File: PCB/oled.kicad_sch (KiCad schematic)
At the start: 5 parts

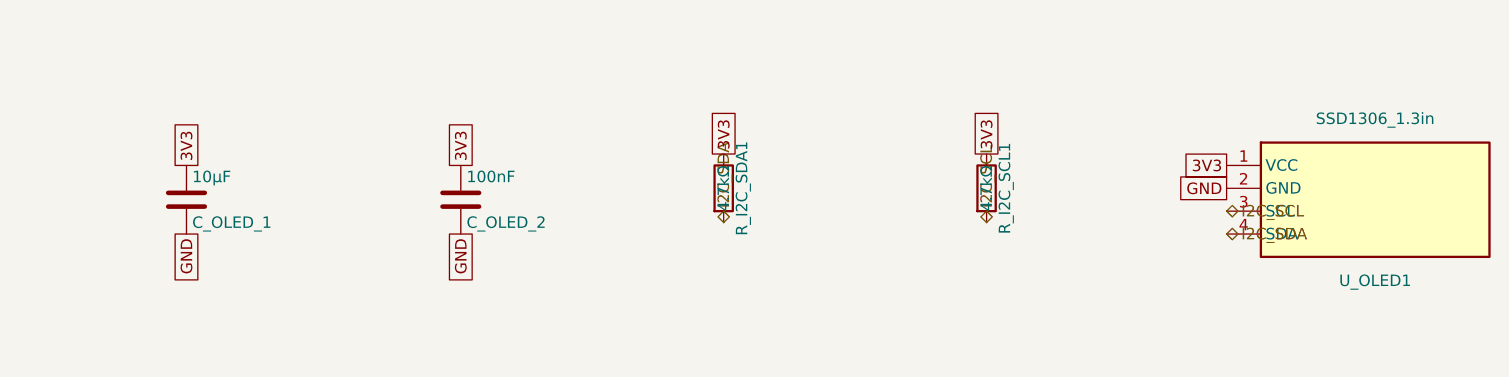
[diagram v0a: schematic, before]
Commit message: Fix footprints and begin layout (#17)
* refactor: updated gulikit footprint

This updates the gulikit thumbstick footprint to be accurate.

* layout: beginning pcb layout

This updates the schematic with a few different footprints while also starts the layout.
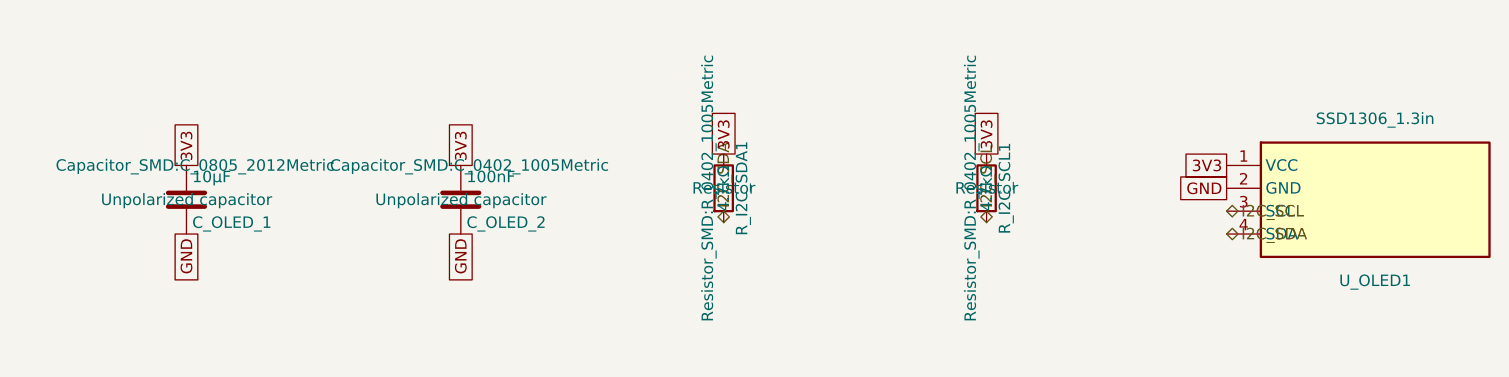
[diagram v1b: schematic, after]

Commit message: refactor: swap footprints and add symmetry
This updates the footprints of a couple components to be smaller and closer to what we want. It also adds two buttons to ensure left and right side symmetry.
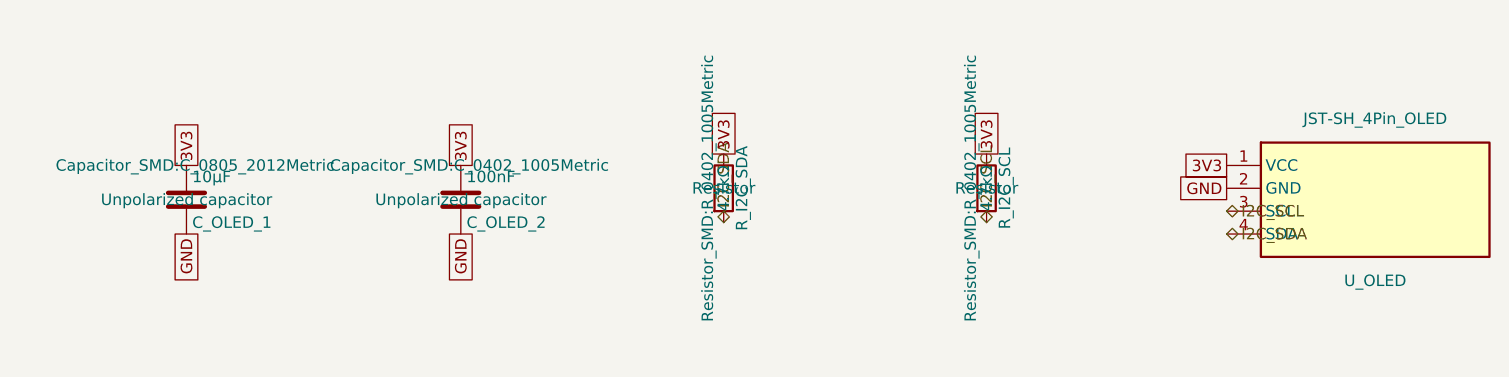
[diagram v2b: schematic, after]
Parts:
- removed R_I2C_SCL1, R_I2C_SDA1: 4.7kΩ, Resistor_SMD:R_0402_1005Metric, symbol Device:R
- removed U_OLED1: SSD1306_1.3in, Display:Adafruit_SSD1306, symbol SnipsControllers:SSD1306_OLED_4pin
- added R_I2C_SCL, R_I2C_SDA: 4.7kΩ, Resistor_SMD:R_0402_1005Metric, symbol Device:R
- added U_OLED: JST-SH_4Pin_OLED, Connector_JST:JST_SH_SM04B-SRSS-TB_1x04-1MP_P1.00mm_Horizontal, symbol SnipsControllers:SSD1306_OLED_4pin
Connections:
- net 3V3: now also R_I2C_SCL.1, R_I2C_SDA.1, U_OLED.1 (VCC)
- net GND: now also U_OLED.2 (GND)
- net I2C_SCL: now also R_I2C_SCL.2, U_OLED.3 (SCL)
- net I2C_SDA: now also R_I2C_SDA.2, U_OLED.4 (SDA)

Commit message: layout: everything is on the board
The board edge cuts are down to 100mm x 35mm. All the components have the right footprints and are on the board, but no traces exist yet, and not all circuits are laid out properly yet. Lots of DRC warnings.
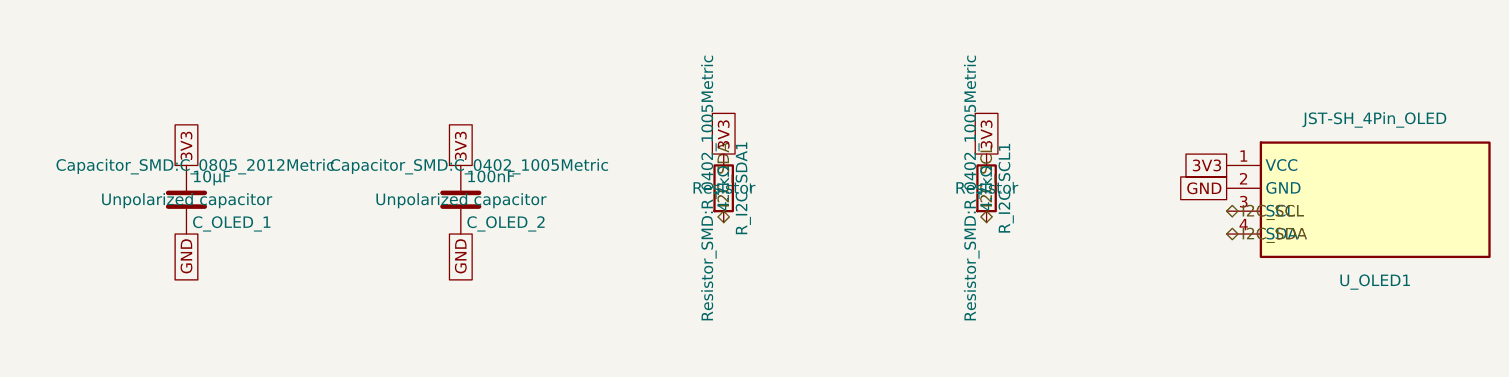
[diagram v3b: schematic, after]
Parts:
- removed R_I2C_SCL, R_I2C_SDA: 4.7kΩ, Resistor_SMD:R_0402_1005Metric, symbol Device:R
- removed U_OLED: JST-SH_4Pin_OLED, Connector_JST:JST_SH_SM04B-SRSS-TB_1x04-1MP_P1.00mm_Horizontal, symbol SnipsControllers:SSD1306_OLED_4pin
- added R_I2C_SCL1, R_I2C_SDA1: 4.7kΩ, Resistor_SMD:R_0402_1005Metric, symbol Device:R
- added U_OLED1: JST-SH_4Pin_OLED, Connector_JST:JST_SH_SM04B-SRSS-TB_1x04-1MP_P1.00mm_Horizontal, symbol SnipsControllers:SSD1306_OLED_4pin
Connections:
- net 3V3: now also R_I2C_SCL1.1, R_I2C_SDA1.1, U_OLED1.1 (VCC)
- net GND: now also U_OLED1.2 (GND)
- net I2C_SCL: now also R_I2C_SCL1.2, U_OLED1.3 (SCL)
- net I2C_SDA: now also R_I2C_SDA1.2, U_OLED1.4 (SDA)

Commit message: task: board is fully routed
That was a pain, but it is all routed and connected now.
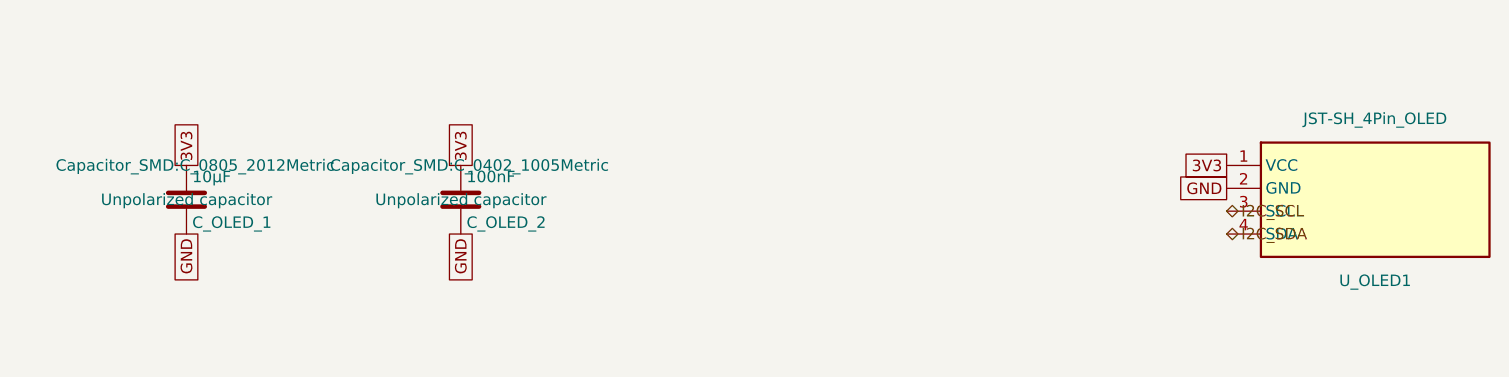
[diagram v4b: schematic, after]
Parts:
- removed R_I2C_SCL1, R_I2C_SDA1: 4.7kΩ, Resistor_SMD:R_0402_1005Metric, symbol Device:R
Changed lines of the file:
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@@
-		)
-	)
-	(global_label "3V3"
-		(shape passive)
-		(at 171.45 100.33 90)
-		(fields_autoplaced yes)
-		(effects
-			(font
-				(size 1.27 1.27)
-			)
-			(justify left)
-		)
-		(property "Intersheetrefs" "${INTERSHEET_REFS}"
-			(at 171.45 100.33 0)
-			(hide yes)
-			(show_name no)
-			(do_not_autoplace no)
-			(effects
-				(font
-					(size 1.27 1.27)
-				)
-			)
-		)
-	)
-	(global_label "3V3"
-		(shape passive)
-		(at 142.24 100.33 90)
-		(fields_autoplaced yes)
-		(effects
-			(font
-				(size 1.27 1.27)
-			)
-			(justify left)
-		)
-		(property "Intersheetrefs" "${INTERSHEET_REFS}"
-			(at 142.24 100.33 0)
-			(hide yes)
-			(show_name no)
-			(do_not_autoplace no)
-			(effects
-				(font
-					(size 1.27 1.27)
-				)
-			)
 		)
 	)
@@
 		(shape bidirectional)
 		(at 198.12 109.22 0)
-		(effects
-			(font
-				(size 1.27 1.27)
-			)
-			(justify left)
-		)
-	)
-	(hierarchical_label "I2C_SDA"
-		(shape bidirectional)
-		(at 142.24 107.95 90)
-		(effects
-			(font
-				(size 1.27 1.27)
-			)
-			(justify left)
-		)
-	)
-	(hierarchical_label "I2C_SCL"
-		(shape bidirectional)
-		(at 171.45 107.95 90)
 		(effects
 			(font
@@
 					(unit 1)
 				)
-			)
-		)
-	)
-	(symbol
-		(lib_id "Device:R")
-		(at 171.45 104.14 0)
-		(unit 1)
-		(body_style 1)
-		(exclude_from_sim no)
-		(in_bom yes)
-		(on_board yes)
-		(in_pos_files yes)
-		(dnp no)
-		(fields_autoplaced yes)
-		(property "Reference" "R_I2C_SCL1"
-			(at 173.482 104.14 90)
-			(show_name no)
-			(do_not_autoplace no)
-			(effects
-				(font
-					(size 1.27 1.27)
-				)
-			)
-		)
-		(property "Value" "4.7kΩ"
-			(at 171.45 104.14 90)
-			(show_name no)
-			(do_not_autoplace no)
-			(effects
-				(font
-					(size 1.27 1.27)
-				)
-			)
-		)
-		(property "Footprint" "Resistor_SMD:R_0402_1005Metric"
-			(at 169.672 104.14 90)
-			(show_name no)
-			(do_not_autoplace no)
-			(effects
-				(font
-					(size 1.27 1.27)
-				)
-			)
-		)
-		(property "Datasheet" ""
-			(at 171.45 104.14 0)
-			(show_name no)
-			(do_not_autoplace no)
-			(effects
-				(font
-					(size 1.27 1.27)
-				)
-			)
-		)
-		(property "Description" "Resistor"
-			(at 171.45 104.14 0)
-			(show_name no)
-			(do_not_autoplace no)
-			(effects
-				(font
-					(size 1.27 1.27)
-				)
-			)
-		)
-		(pin "1"
-		)
-		(pin "2"
-		)
-		(instances
-			(project "snips_controller"
-				(path "/21935953-32a0-46ad-8079-8177920c6978/ab30dd66-bbd7-4b32-bf8e-8b7d2bf83841"
-					(reference "R_I2C_SCL1")
-					(unit 1)
-				)
-			)
-		)
-	)
-	(symbol
-		(lib_id "Device:R")
-		(at 142.24 104.14 0)
-		(unit 1)
-		(body_style 1)
-		(exclude_from_sim no)
-		(in_bom yes)
-		(on_board yes)
-		(in_pos_files yes)
-		(dnp no)
-		(fields_autoplaced yes)
-		(property "Reference" "R_I2C_SDA1"
-			(at 144.272 104.14 90)
-			(show_name no)
-			(do_not_autoplace no)
-			(effects
-				(font
-					(size 1.27 1.27)
-				)
-			)
-		)
-		(property "Value" "4.7kΩ"
-			(at 142.24 104.14 90)
-			(show_name no)
-			(do_not_autoplace no)
-			(effects
-				(font
-					(size 1.27 1.27)
-				)
-			)
-		)
-		(property "Footprint" "Resistor_SMD:R_0402_1005Metric"
-			(at 140.462 104.14 90)
-			(show_name no)
-			(do_not_autoplace no)
-			(effects
-				(font
-					(size 1.27 1.27)
-				)
-			)
-		)
-		(property "Datasheet" ""
-			(at 142.24 104.14 0)
-			(show_name no)
-			(do_not_autoplace no)
-			(effects
-				(font
-					(size 1.27 1.27)
-				)
-			)
-		)
-		(property "Description" "Resistor"
-			(at 142.24 104.14 0)
-			(show_name no)
-			(do_not_autoplace no)
-			(effects
-				(font
-					(size 1.27 1.27)
-				)
-			)
-		)
-		(pin "1"
-		)
-		(pin "2"
-		)
-		(instances
-			(project "snips_controller"
-				(path "/21935953-32a0-46ad-8079-8177920c6978/ab30dd66-bbd7-4b32-bf8e-8b7d2bf83841"
-					(reference "R_I2C_SDA1")
-					(unit 1)
-				)

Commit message: task: part number populated (#26)
kicad-happy run part 2 - MPN numbers populated
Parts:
- C_OLED_1: MF (none) -> Yageo; Manufacturer_Part_Number (none) -> CC0805KRX5R7BB106
- C_OLED_2: MF (none) -> Yageo; Manufacturer_Part_Number (none) -> CC0402KRX7R9BB104
- U_OLED1: MF (none) -> JST; Manufacturer_Part_Number (none) -> SM04B-SRSS-TB
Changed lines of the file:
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@@
+			)
+		)
+		(property "MF" "JST" (at 0 0 0)
+			(effects
+				(font
+					(size 1.27 1.27)
+				)
+				(hide yes)
+			)
+		)
+		(property "Manufacturer_Part_Number" "SM04B-SRSS-TB" (at 0 0 0)
+			(effects
+				(font
+					(size 1.27 1.27)
+				)
+				(hide yes)
 			)
 		)
@@
 			)
 		)
+		(property "MF" "Yageo" (at 0 0 0)
+			(effects
+				(font
+					(size 1.27 1.27)
+				)
+				(hide yes)
+			)
+		)
+		(property "Manufacturer_Part_Number" "CC0805KRX5R7BB106" (at 0 0 0)
+			(effects
+				(font
+					(size 1.27 1.27)
+				)
+				(hide yes)
+			)
+		)
 		(pin "1"
 		)
@@
 			)
 		)
+		(property "MF" "Yageo" (at 0 0 0)
+			(effects
+				(font
+					(size 1.27 1.27)
+				)
+				(hide yes)
+			)
+		)
+		(property "Manufacturer_Part_Number" "CC0402KRX7R9BB104" (at 0 0 0)
+			(effects
+				(font
+					(size 1.27 1.27)
+				)
+				(hide yes)
+			)
+		)

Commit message: task: more gerbers
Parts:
- U_OLED1: Manufacturer_Part_Number SM04B-SRSS-TB -> SM04B-SRSS-TB(LF)(SN)
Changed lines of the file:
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@@
 			)
 		)
-		(property "Manufacturer_Part_Number" "SM04B-SRSS-TB"
+		(property "Manufacturer_Part_Number" "SM04B-SRSS-TB(LF)(SN)"
 			(at 0 0 0)
 			(hide yes)
